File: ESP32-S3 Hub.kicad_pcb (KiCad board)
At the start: 6 copper layers, 15 x 30 mm, 73 parts, among them J1 Precidip 853-87-004-20-001101, J10 Precidip 853-87-004-20-001101, J11 FPC 0.3mm Aces 51688-0070M, J12 Precidip 853-87-004-20-001101, J13 TE 3-2363961-0 receptacle, J15 Precidip 853-87-004-20-001101, J16 TE 3-2363961-0 receptacle, J18 Precidip 852-10-004-20-001101, J2 Precidip 853-87-004-20-001101, J3 FPC 0.3mm Aces 51688-0070M, J4 Precidip 853-87-004-20-001101, J5 FPC 0.3mm Aces 51688-0070M, J6 Precidip 853-87-004-20-001101, J7 Precidip 853-87-004-20-001101, J8 FPC 0.3mm Aces 51688-0070M, J9 Precidip 853-87-004-20-001101, SW1 Mitsumi R-667996, SW2 Mitsumi R-667996, U1 ESP32-S3 FN8, U2 SN74LV595A, U3 THVD1420DRLR, U4 TPS2521ARPWR, U5 SN74LV595A, U6 TS5A3159DCK, Y1 2 pin 40MHZ, 10ppm tol., 20pp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

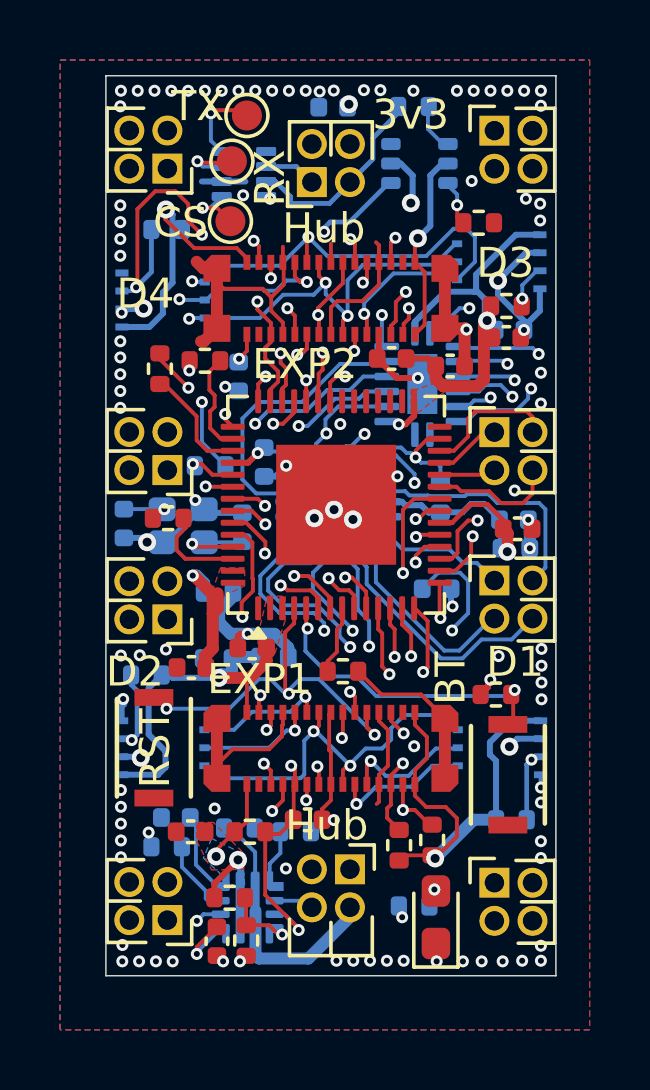
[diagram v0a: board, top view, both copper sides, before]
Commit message: Aggressive reroute 1 for proper connection
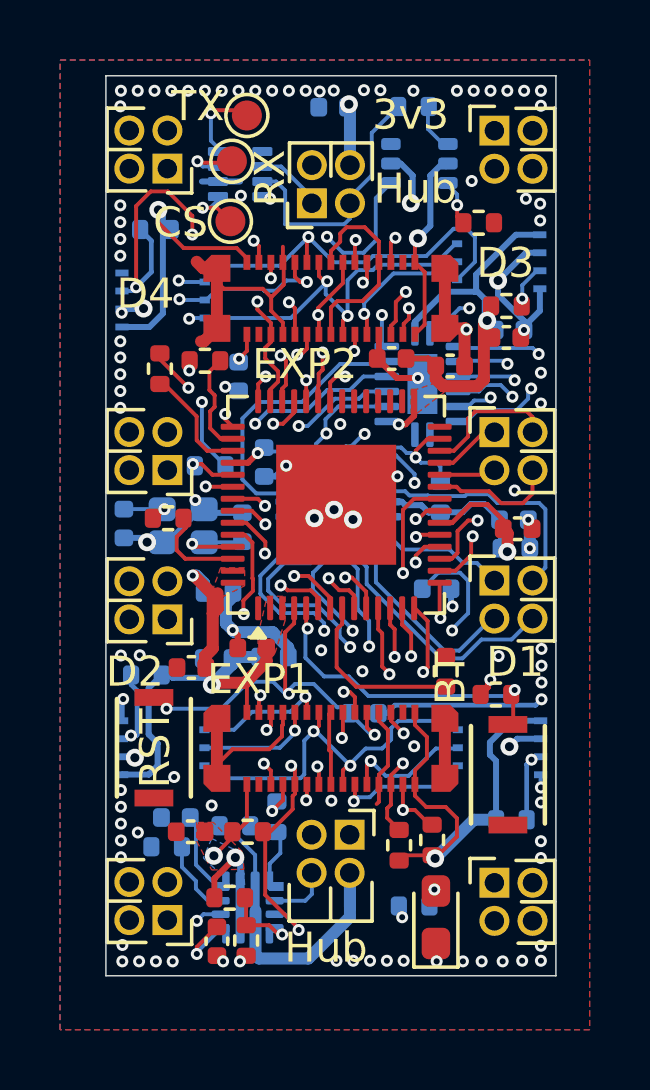
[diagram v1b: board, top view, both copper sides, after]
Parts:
- C13: moved to B.Cu
- moved C13 4.01 mm to (156.5, 103.0)
- moved R1 3.42 mm to (159.2, 101.7), turned to 90 degrees
- moved J18 1.15 mm to (156.0, 107.1)
- moved R12 0.80 mm to (153.6, 106.5), turned to -90 degrees
- moved J12 0.70 mm to (154.8, 86.0)
- moved R20 0.38 mm to (149.6, 86.9)
- moved R11 0.17 mm to (152.2, 106.8)
- moved U3 0.12 mm to (152.4, 85.1)
- moved R7 0.07 mm to (152.6, 107.0)
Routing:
- net Free-2: track 13.0 -> 19.2 mm
- net CS-2: track 30.5 -> 26.2 mm
- net SDA: track 40.8 -> 44.7 mm
- net Net-(U1-GPIO3): track 2.18 -> 5.82 mm
- net MOSI: track 60.3 -> 62.8 mm
- net GND: track 82.8 -> 85.2 mm, vias 103 -> 102
- net VBUS: track 8.96 -> 11.1 mm
- net VDD: track 85.7 -> 87.5 mm
- net RS485+: track 35.8 -> 37.3 mm
- net LED: track 24.0 -> 24.6 mm, vias 2 -> 4
